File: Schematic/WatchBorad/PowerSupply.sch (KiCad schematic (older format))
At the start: 21 parts, among them J1 TYPE-C-31-M-17, U1 BQ21040DBVT, U2 TPS2115APWR, U3 MAX809STRG, U4 TPS62740DSST, U5 STC3100IQT

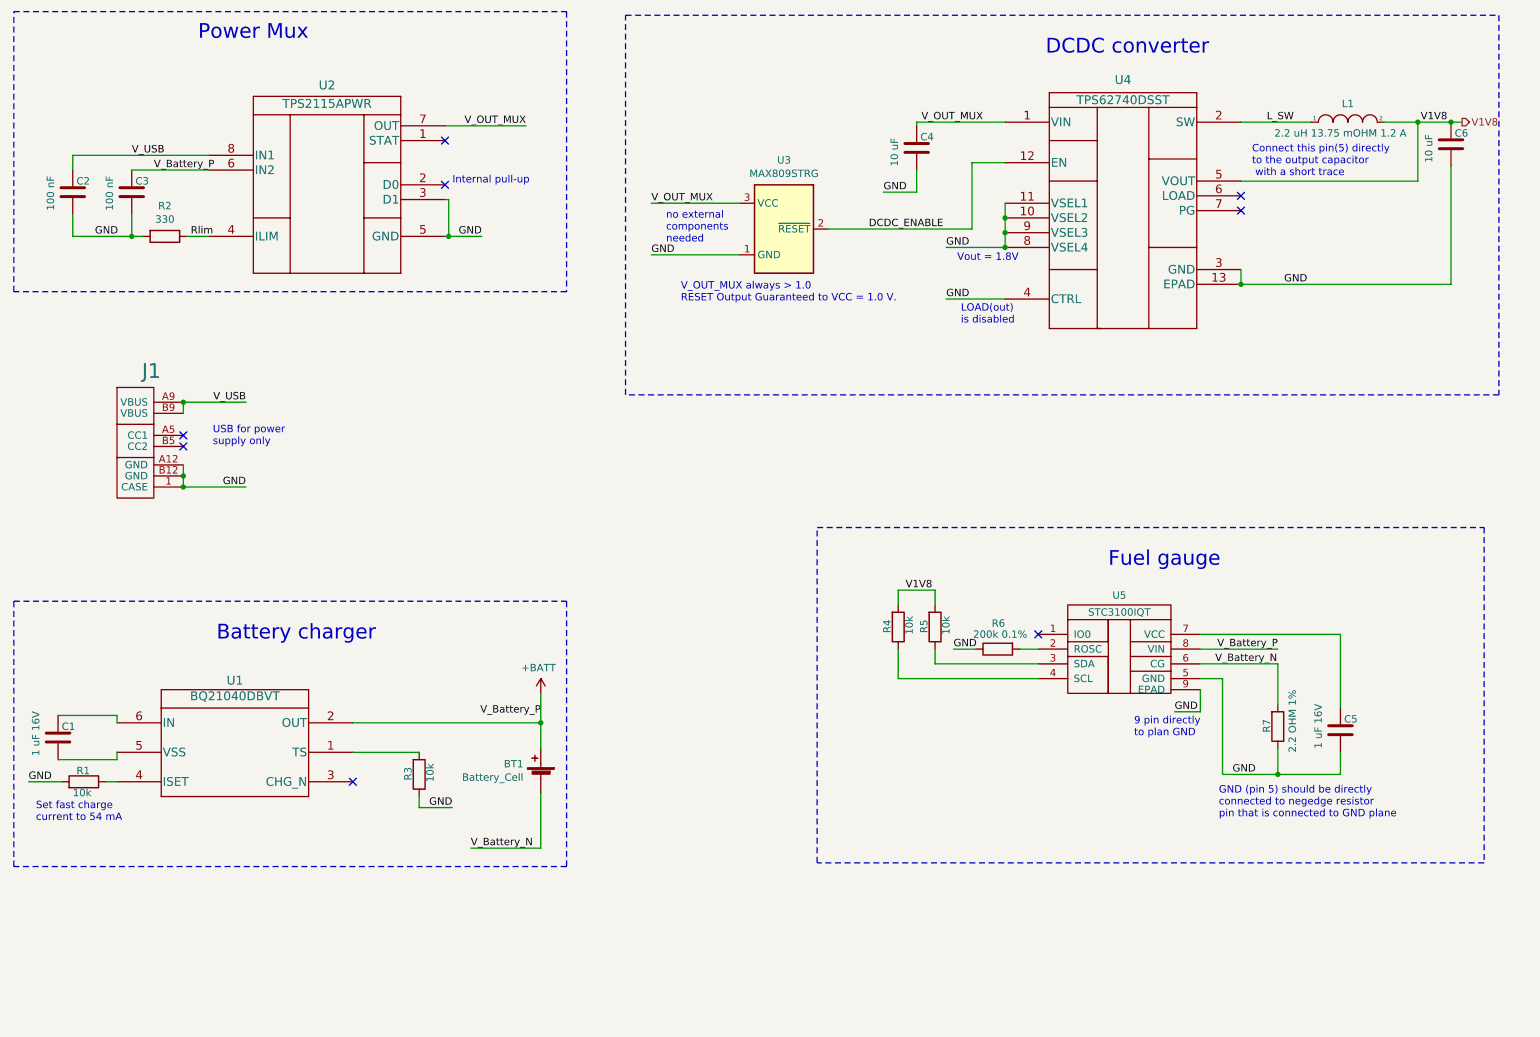
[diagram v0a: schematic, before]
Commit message: Added on/off circuit for PON and added other changes
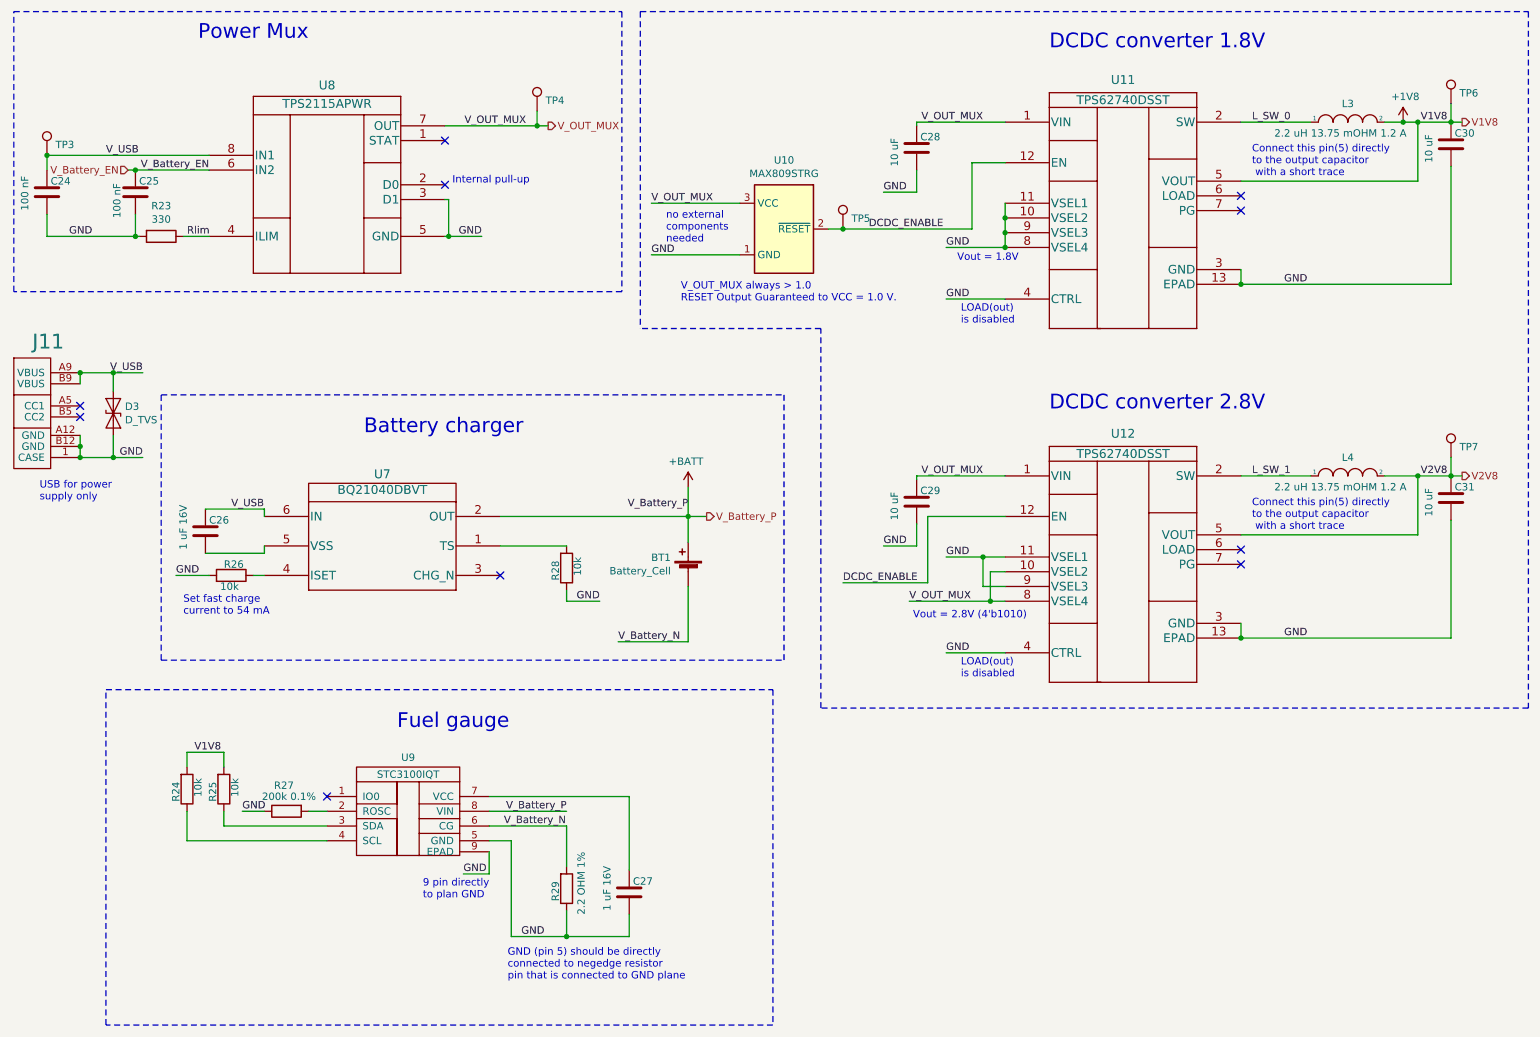
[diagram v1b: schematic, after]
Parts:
- added C29, C31: 10 uF, Capacitors_SMD:C_0603_HandSoldering, symbol Device:C
- added D3: D_TVS, symbol Device:D_TVS
- added L4: 2.2 uH 13.75 mOHM 1.2 A, symbol pspice:INDUCTOR
- added TP3, TP4, TP5, TP6, TP7: TestPoint, testpoints:testpoint, symbol Connector:TestPoint
- added U12: TPS62740DSST, Housings_SON:WSON-12-1EP_3x2mm_Pitch0.5mm, symbol DCDC_Local:TPS62740DSST
- renumbered C2 to C24, C3 to C25, C1 to C26, C5 to C27, C4 to C28, C6 to C30, J1 to J11, L1 to L3, R2 to R23, R4 to R24, R5 to R25, R1 to R26, R6 to R27, R3 to R28, R7 to R29, U3 to U10, U4 to U11, U1 to U7, U2 to U8, U5 to U9
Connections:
- net +BATT: no longer C25.1, U8.6 (IN2)
- net DCDC_ENABLE: now also TP5.1, U12.12 (EN)
- net GND: now also C29.2, C31.2, D3.2 (A2), U12.11 (VSEL1), U12.13 (EPAD), U12.3 (GND), U12.4 (CTRL), U12.9 (VSEL3)
- net V_OUT_MUX: now also C29.1, TP4.1, U12.1 (VIN), U12.10 (VSEL2), U12.8 (VSEL4)
- net V_USB: now also C26.1, U7.6 (IN), D3.1 (A1), TP3.1
- net L_SW renamed L_SW_0
- net V1V8 renamed +1V8
- net +1V8: now also TP6.1
- new net L_SW_1: L4.1, U12.2 (SW)
- new net V2V8: C31.1, L4.2, TP7.1, U12.5 (VOUT)
- new net V_Battery_EN: C25.1, U8.6 (IN2)
- no-connect marks 8 -> 10
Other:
- note added: "DCDC converter 1.8V\n\n"
- note added: "DCDC converter 2.8V\n\n"
- note added: "Vout = 2.8V (4'b1010)\n"
- note removed: "DCDC converter\n"
- moved on the sheet: BT1, C24, C25, C26, C27, J11, R23, R24, R25, R26, R27, R28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
